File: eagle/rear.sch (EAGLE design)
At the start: 11 parts, among them T1 BC846, T2 BC846, T3 BC846

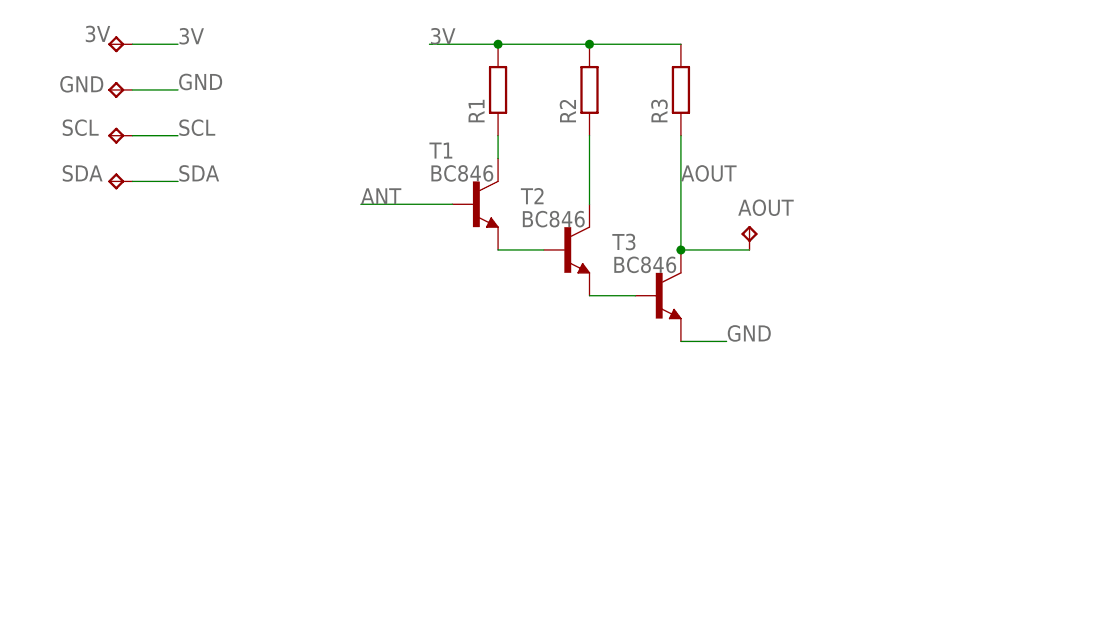
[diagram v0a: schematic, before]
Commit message: Updated probe and rear eagle files
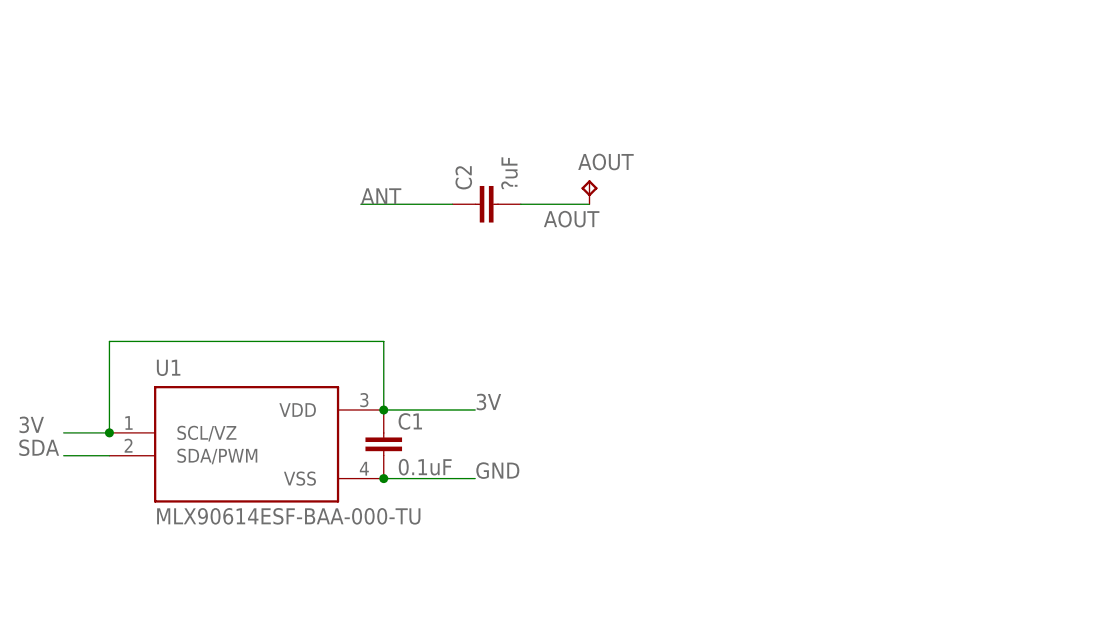
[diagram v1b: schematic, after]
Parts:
- removed 3V, GND, SCL, SDA: TPTP10R, testpad:TPTP10R
- removed R1, R2, R3: (no value), resistor:R-EU_R0805
- removed T1, T2, T3: BC846, transistor:BC846
- added C1: 0.1uF, resistor:C-EUC0805
- added C2: ?uF, resistor:C-EUC0805
- added U1: MLX90614ESF-BAA-000-TU, MLX90614ESF-BAA-000-TU:MLX90614ESF-BAA-000-TU
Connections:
- removed net N$1: T1.E, T2.B
- removed net N$2: T2.E, T3.B
- removed net N$3: R1.1, T1.C
- removed net N$4: R2.1, T2.C
- removed net SCL: SCL.TP
- net 3V: now also C1.1, U1.SCL/VZ, U1.VDD; no longer 3V.TP, R1.2, R2.2, R3.2
- net ANT: now also C2.1; no longer T1.B
- net AOUT: now also C2.2; no longer R3.1, T3.C
- net GND: now also C1.2, U1.VSS; no longer GND.TP, T3.E
- net SDA: now also U1.SDA/PWM; no longer SDA.TP
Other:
- moved on the sheet: AOUT

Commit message: new pcbs
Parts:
- removed AOUT: TPTP10R, testpad:TPTP10R
- removed C2: ?uF, resistor:C-EUC0805
- added ANT: TPTP10R, testpad:TPTP10R
- added R1: 10k, rcl:R-EU_R0805
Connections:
- removed net AOUT: AOUT.TP, C2.2
- new net SCL: R1.1, U1.SCL/VZ
- net 3V: now also R1.2; no longer U1.SCL/VZ
- net ANT: now also ANT.TP; no longer C2.1
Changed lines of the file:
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@@
 </classes>
 <parts>
-<part name="AOUT" library="testpad" library_urn="urn:adsk.eagle:library:385" deviceset="TP" device="TP10R" package3d_urn="urn:adsk.eagle:package:27959/1"/>
+<part name="ANT" library="testpad" library_urn="urn:adsk.eagle:library:385" deviceset="TP" device="TP10R" package3d_urn="urn:adsk.eagle:package:27959/1"/>
 <part name="U1" library="MLX90614ESF-BAA-000-TU" deviceset="MLX90614ESF-BAA-000-TU" device=""/>
 <part name="C1" library="resistor" library_urn="urn:adsk.eagle:library:348" deviceset="C-EU" device="C0805" package3d_urn="urn:adsk.eagle:package:23617/2" value="0.1uF"/>
-<part name="C2" library="resistor" library_urn="urn:adsk.eagle:library:348" deviceset="C-EU" device="C0805" package3d_urn="urn:adsk.eagle:package:23617/2" value="?uF"/>
+<part name="R1" library="rcl" library_urn="urn:adsk.eagle:library:334" deviceset="R-EU_" device="R0805" package3d_urn="urn:adsk.eagle:package:23553/2" value="10k"/>
 </parts>
 <sheets>
@@
 </plain>
 <instances>
-<instance part="AOUT" gate="G$1" x="38.1" y="48.26" smashed="yes">
-<attribute name="NAME" x="36.83" y="49.53" size="1.778" layer="95"/>
-<attribute name="TP_SIGNAL_NAME" x="39.37" y="46.99" size="1.778" layer="97"/>
+<instance part="ANT" gate="G$1" x="22.86" y="48.26" smashed="yes">
+<attribute name="NAME" x="21.59" y="49.53" size="1.778" layer="95"/>
+<attribute name="TP_SIGNAL_NAME" x="24.13" y="46.99" size="1.778" layer="97"/>
 </instance>
 <instance part="U1" gate="G$1" x="0" y="20.32" smashed="yes">
@@
 <attribute name="VALUE" x="16.764" y="15.621" size="1.778" layer="96"/>
 </instance>
-<instance part="C2" gate="G$1" x="25.4" y="45.72" smashed="yes" rot="R90">
-<attribute name="NAME" x="25.019" y="47.244" size="1.778" layer="95" rot="R90"/>
-<attribute name="VALUE" x="30.099" y="47.244" size="1.778" layer="96" rot="R90"/>
+<instance part="R1" gate="G$1" x="0" y="30.48" smashed="yes">
+<attribute name="NAME" x="-3.81" y="31.9786" size="1.778" layer="95"/>
+<attribute name="VALUE" x="1.27" y="32.258" size="1.778" layer="96"/>
 </instance>
 </instances>
@@
 <wire x1="22.86" y1="45.72" x2="12.7" y2="45.72" width="0.1524" layer="91"/>
 <label x="12.7" y="45.72" size="1.778" layer="95"/>
-<pinref part="C2" gate="G$1" pin="1"/>
+<pinref part="ANT" gate="G$1" pin="TP"/>
 </segment>
 </net>
 <net name="3V" class="0">
 <segment>
-<pinref part="U1" gate="G$1" pin="SCL/VZ"/>
-<wire x1="-15.24" y1="20.32" x2="-20.32" y2="20.32" width="0.1524" layer="91"/>
-<label x="-25.4" y="20.32" size="1.778" layer="95"/>
-<wire x1="-15.24" y1="20.32" x2="-15.24" y2="30.48" width="0.1524" layer="91"/>
-<junction x="-15.24" y="20.32"/>
 <pinref part="U1" gate="G$1" pin="VDD"/>
 <wire x1="15.24" y1="22.86" x2="25.4" y2="22.86" width="0.1524" layer="91"/>
 <label x="25.4" y="22.86" size="1.778" layer="95"/>
-<wire x1="-15.24" y1="30.48" x2="15.24" y2="30.48" width="0.1524" layer="91"/>
 <wire x1="15.24" y1="30.48" x2="15.24" y2="22.86" width="0.1524" layer="91"/>
 <junction x="15.24" y="22.86"/>
 <pinref part="C1" gate="G$1" pin="1"/>
+<pinref part="R1" gate="G$1" pin="2"/>
+<wire x1="5.08" y1="30.48" x2="15.24" y2="30.48" width="0.1524" layer="91"/>
 </segment>
 </net>
@@
 </segment>
 </net>
-<net name="AOUT" class="0">
-<segment>
-<pinref part="AOUT" gate="G$1" pin="TP"/>
-<wire x1="30.48" y1="45.72" x2="38.1" y2="45.72" width="0.1524" layer="91"/>
-<label x="33.02" y="43.18" size="1.778" layer="95"/>
-<pinref part="C2" gate="G$1" pin="2"/>
-</segment>
-</net>
 <net name="SDA" class="0">
 <segment>
@@
 <wire x1="-15.24" y1="17.78" x2="-20.32" y2="17.78" width="0.1524" layer="91"/>
 <label x="-25.4" y="17.78" size="1.778" layer="95"/>
+</segment>
+</net>
+<net name="SCL" class="0">
+<segment>
+<pinref part="U1" gate="G$1" pin="SCL/VZ"/>
+<wire x1="-15.24" y1="20.32" x2="-15.24" y2="30.48" width="0.1524" layer="91"/>
+<junction x="-15.24" y="20.32"/>
+<wire x1="-15.24" y1="20.32" x2="-20.32" y2="20.32" width="0.1524" layer="91"/>
+<label x="-25.4" y="20.32" size="1.778" layer="95"/>
+<pinref part="R1" gate="G$1" pin="1"/>
+<wire x1="-15.24" y1="30.48" x2="-5.08" y2="30.48" width="0.1524" layer="91"/>
 </segment>
 </net>
@@
 packages will not be understood (or retained) with this version.
 </note>
+<note version="8.4" severity="warning">
+Since Version 8.4, EAGLE supports properties for SPICE simulation.
+Probes in schematics and SPICE mapping objects found in parts and library devices
+will not be understood with this version. Update EAGLE to the latest version
+for full support of SPICE simulation.
+</note>
 </compatibility>

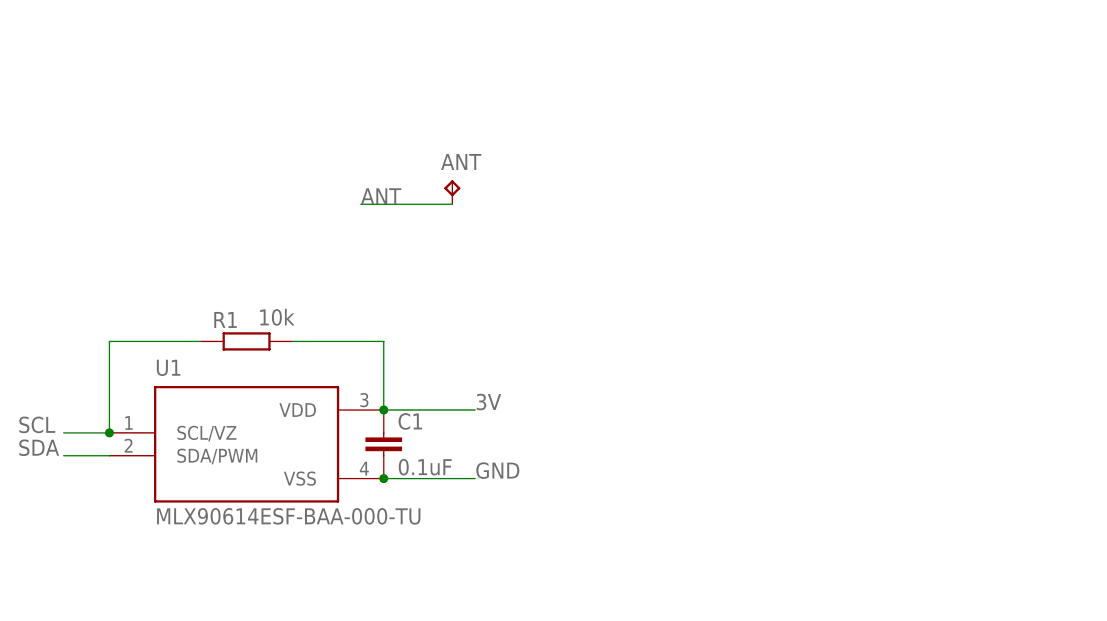
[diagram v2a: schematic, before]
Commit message: added encoder to rear pcb
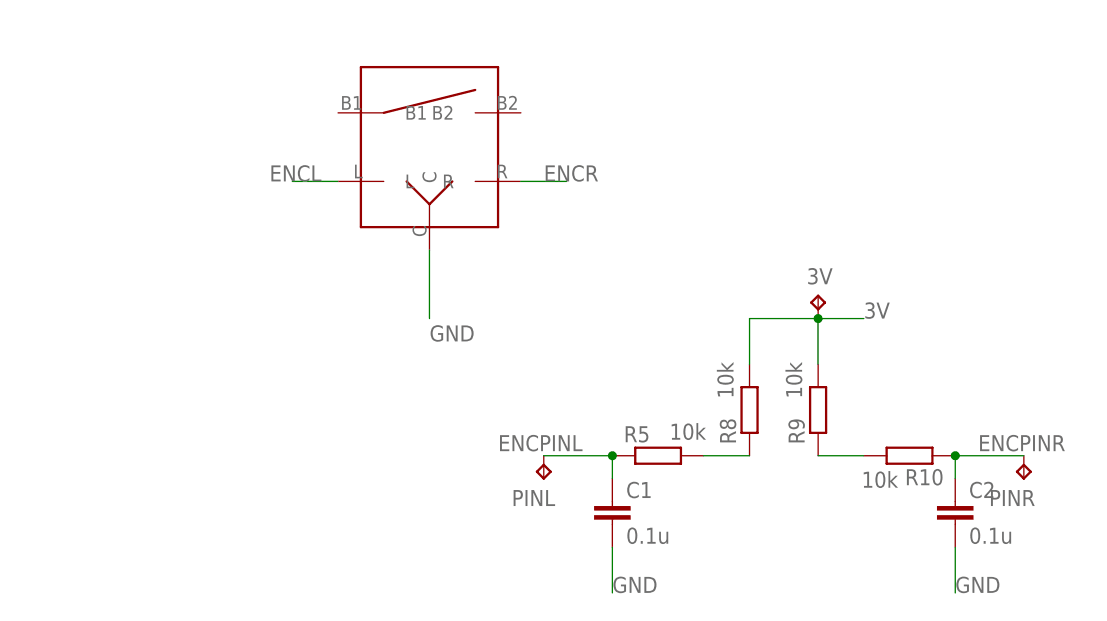
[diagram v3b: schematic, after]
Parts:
- removed ANT: TPTP10R, testpad:TPTP10R
- removed R1: 10k, rcl:R-EU_R0805
- removed U1: MLX90614ESF-BAA-000-TU, MLX90614ESF-BAA-000-TU:MLX90614ESF-BAA-000-TU
- added 3V, PINL, PINR: TPTP14R, testpad:TPTP14R
- added C2: 0.1u, resistor:C-EUC0805
- added R10, R5, R8, R9: 10k, resistor:R-EU_M0805
- added U$1: ENCODER, general:ENCODER
- C1: value 0.1uF -> 0.1u
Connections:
- removed net ANT: ANT.TP
- removed net SCL: R1.1, U1.SCL/VZ
- removed net SDA: U1.SDA/PWM
- new net ENCL: R5.2, R8.1, U$1.L
- new net ENCPINL: C1.1, PINL.TP, R5.1
- new net ENCPINR: C2.1, PINR.TP, R10.1
- new net ENCR: R10.2, R9.1, U$1.R
- net 3V: now also 3V.TP, R8.2, R9.2; no longer C1.1, R1.2, U1.VDD
- net GND: now also C2.2, U$1.C; no longer U1.VSS
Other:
- moved on the sheet: C1
